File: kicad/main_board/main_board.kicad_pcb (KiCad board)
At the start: 4 copper layers, 198.1 x 61 mm, 271 parts, among them J1 USB_C, J10 LINE_ALT, J11 LINE, J12 DRV, J13 DRV_PWR, J14 CH_IN, J15 CH1, J16 CH2, J17 CH3, J18 CH4, J2 TRIG_A, J3 TRIG_B, J4 BAT, J5 BAT_LINK, J6 FRONT_PANEL, J7 I2C, J8 SWD, J9 MIC, Q1 DMP3018SFV, Q10 AO3401A, Q2 AO3400A, Q3 CSD17551Q3A, Q4 CSD17551Q3A, Q5 CSD17551Q3A, Q6 CSD17551Q3A, Q7 CSD25402Q3A, Q8 AO3400A, Q9 DMP3018SFV, SW1 PWR, U1 SRV05-4, U10 MCP4451-503, U11 MCP6002, U12 MCP6002, U2 SRV05-4, U3 FUSB302B, U4 BQ25703A, U5 TPS560430, U6 TPS560430, U7 MCP4728, U8 RP2040, U9 W25Q128JVS, Y1 12MHz

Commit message: fix title block
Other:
- board text added: "${TITLE} ${PROJECTNAME} rev${REVISION} ${hash}"
- board text removed: "SW32 ${PROJECTNAME} rev${REVISION} ${hash}"
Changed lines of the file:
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@@
 	(paper "A4")
 	(title_block
-		(title "SW32 - Main Board")
-		(date "2024-06-11")
+		(title "SW32")
+		(date "2024-06-12")
 		(rev "1")
 		(company "saawsm")
@@
 		(layer "Edge.Cuts")
 	)
-	(gr_text "SW32\n${PROJECTNAME}\nrev${REVISION} ${hash}\n"
+	(gr_text "${TITLE}\n${PROJECTNAME}\nrev${REVISION} ${hash}\n"
 		(locked yes)
 		(at 223.647 88.646 0)
@@
 	(dimension
 		(type orthogonal)
+		(locked yes)
 		(layer "Dwgs.User")
 		(pts
@@
 		(orientation 0)
 		(gr_text "198.1200 mm"
+			(locked yes)
 			(at 149.86 58.74 0)
 			(layer "Dwgs.User")
@@
 	(dimension
 		(type orthogonal)
+		(locked yes)
 		(layer "Dwgs.User")
 		(pts
@@
 		(orientation 1)
 		(gr_text "60.9600 mm"
+			(locked yes)
 			(at 267.02 96.52 90)
 			(layer "Dwgs.User")

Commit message: add plot settings
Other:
- board text added: "${TITLE} ${PROJECTNAME} rev${REVISION}"
- board text removed: "${TITLE} ${PROJECTNAME} rev${REVISION} ${hash}"
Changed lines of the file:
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@@
 			(plot_on_all_layers_selection 0x0000000_00000000)
 			(disableapertmacros no)
-			(usegerberextensions no)
-			(usegerberattributes yes)
-			(usegerberadvancedattributes yes)
-			(creategerberjobfile yes)
+			(usegerberextensions yes)
+			(usegerberattributes no)
+			(usegerberadvancedattributes no)
+			(creategerberjobfile no)
 			(dashed_line_dash_ratio 12.000000)
 			(dashed_line_gap_ratio 3.000000)
@@
 			(plotinvisibletext no)
 			(sketchpadsonfab no)
-			(subtractmaskfromsilk no)
+			(subtractmaskfromsilk yes)
 			(outputformat 1)
 			(mirror no)
-			(drillshape 1)
+			(drillshape 0)
 			(scaleselection 1)
-			(outputdirectory "")
+			(outputdirectory "../../pcb/main_board/")
 		)
 	)
@@
 		(layer "Edge.Cuts")
 	)
-	(gr_text "${TITLE}\n${PROJECTNAME}\nrev${REVISION} ${hash}\n"
+	(gr_text "${TITLE}\n${PROJECTNAME}\nrev${REVISION}\n"
 		(locked yes)
 		(at 223.647 88.646 0)

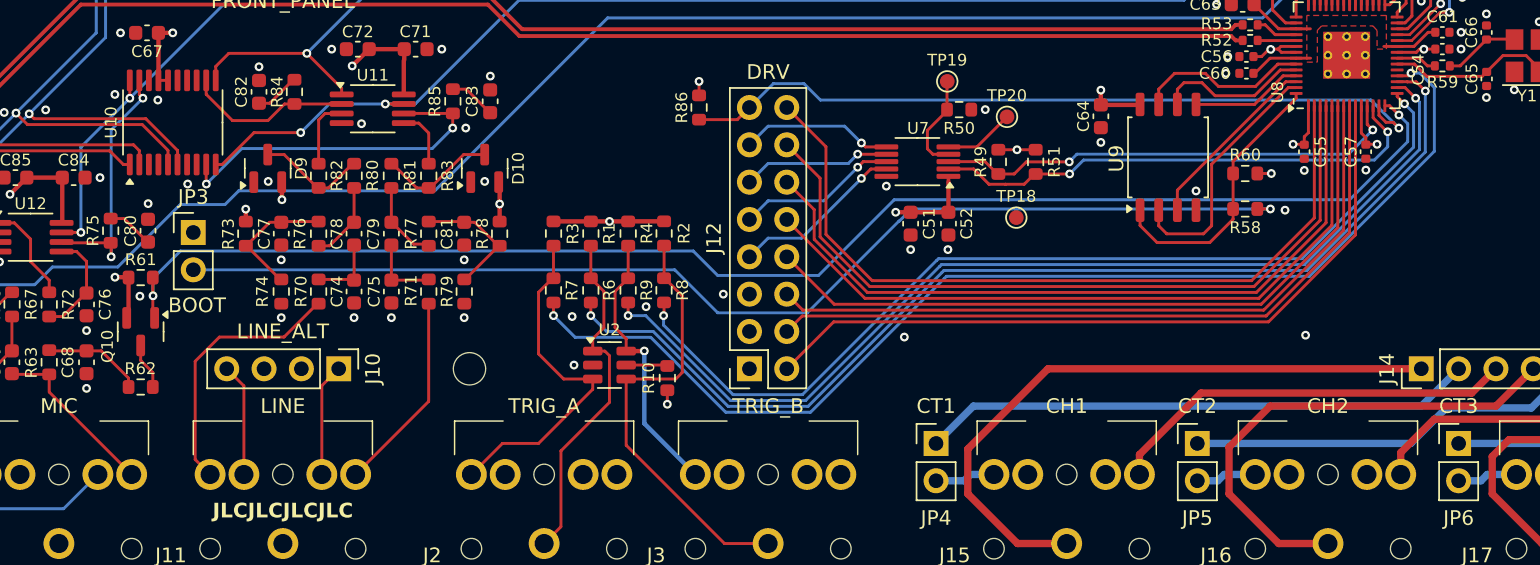
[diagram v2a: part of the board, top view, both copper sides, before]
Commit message: add missing vias
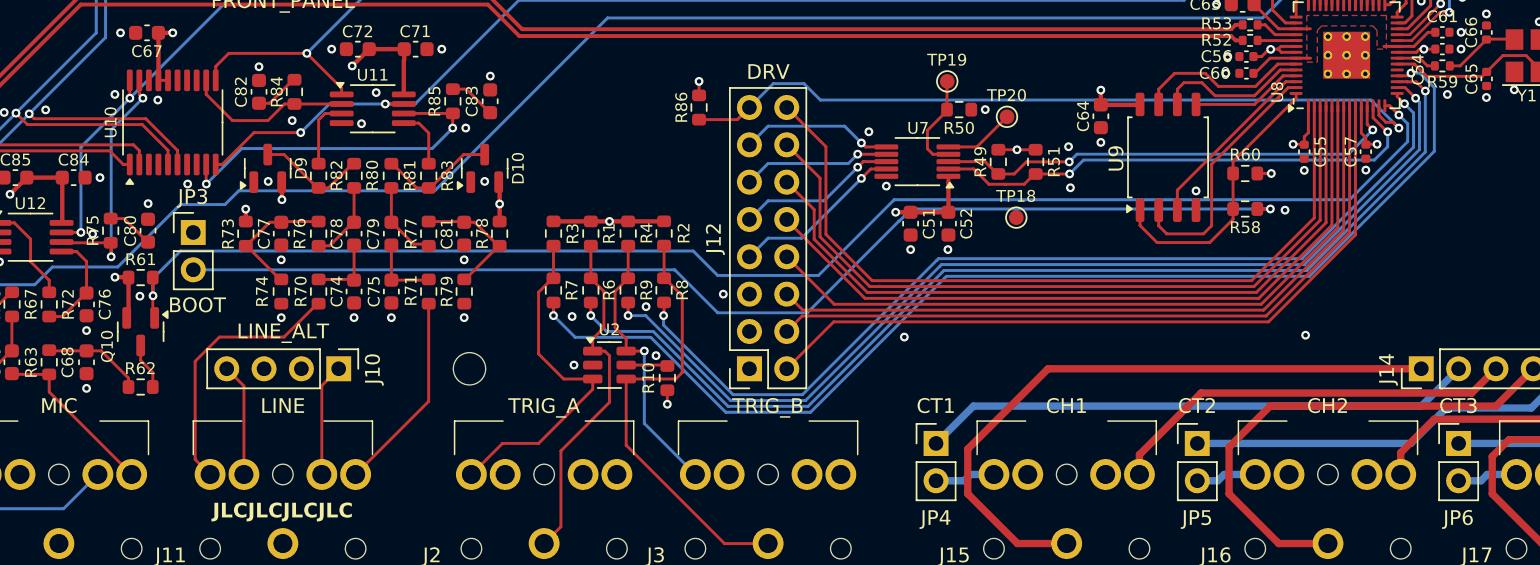
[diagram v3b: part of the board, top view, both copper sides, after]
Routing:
- net GND: vias 266 -> 274
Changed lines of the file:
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@@
 	(title_block
 		(title "SW32")
-		(date "2024-06-12")
+		(date "2024-06-19")
 		(rev "1")
 		(company "saawsm")
@@
 	)
 	(via
+		(at 169.418 95.631)
+		(size 0.6)
+		(drill 0.3)
+		(layers "F.Cu" "B.Cu")
+		(locked yes)
+		(free yes)
+		(net 2)
+	)
+	(via
 		(at 79.629 84.582)
 		(size 0.6)
@@
 	)
 	(via
+		(at 135.89 92.964)
+		(size 0.6)
+		(drill 0.3)
+		(layers "F.Cu" "B.Cu")
+		(locked yes)
+		(free yes)
+		(net 2)
+	)
+	(via
 		(at 211.441452 87.611129)
 		(size 0.6)
@@
 	)
 	(via
+		(at 154.935387 110.866225)
+		(size 0.6)
+		(drill 0.3)
+		(layers "F.Cu" "B.Cu")
+		(locked yes)
+		(free yes)
+		(net 2)
+	)
+	(via
+		(at 183.134 99.441)
+		(size 0.6)
+		(drill 0.3)
+		(layers "F.Cu" "B.Cu")
+		(locked yes)
+		(free yes)
+		(net 2)
+	)
+	(via
 		(at 185.928 66.675)
 		(size 0.6)
@@
 	)
 	(via
+		(at 116.590536 102.588)
+		(size 0.6)
+		(drill 0.3)
+		(layers "F.Cu" "B.Cu")
+		(locked yes)
+		(free yes)
+		(net 2)
+	)
+	(via
 		(at 56.556266 121.319389)
 		(size 0.6)
@@
 	)
 	(via
+		(at 130.175 94.869)
+		(size 0.6)
+		(drill 0.3)
+		(layers "F.Cu" "B.Cu")
+		(locked yes)
+		(free yes)
+		(net 2)
+	)
+	(via
 		(at 51.477 98.46)
 		(size 0.6)
@@
 	)
 	(via
+		(at 183.007 96.647)
+		(size 0.6)
+		(drill 0.3)
+		(layers "F.Cu" "B.Cu")
+		(locked yes)
+		(free yes)
+		(net 2)
+	)
+	(via
 		(at 101.346 88.011)
 		(size 0.6)
@@
 	)
 	(via
+		(at 208.788 93.091)
+		(size 0.6)
+		(drill 0.3)
+		(layers "F.Cu" "B.Cu")
+		(locked yes)
+		(free yes)
+		(net 2)
+	)
+	(via
 		(at 70.088716 112.456263)
 		(size 0.6)
@@
 		(start 152.9025 110.556)
 		(end 154.129223 110.556)
-		(width 0.3)
+		(width 0.2)
 		(locked yes)
 		(layer "F.Cu")
@@
 		(start 154.137066 115.479066)
 		(end 157.61 118.952)
-		(width 0.3)
+		(width 0.2)
 		(locked yes)
 		(layer "B.Cu")
@@
 		(start 154.137066 110.548157)
 		(end 154.137066 115.479066)
-		(width 0.3)
+		(width 0.2)
 		(locked yes)
 		(layer "B.Cu")
